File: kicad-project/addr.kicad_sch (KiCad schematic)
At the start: 0 parts

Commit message: address register and more
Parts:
- added U? (x2): 74LS173, symbol 74xx:74LS173
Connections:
- new net: U?.10 (E2), U?.9 (E1) (x2)
- new net CLK: U?.7 (Cp), U?.7 (Cp)
- new net GND: U?.1 (Oe1), U?.1 (Oe1), U?.2 (Oe2), U?.2 (Oe2), U?.8 (GND), U?.8 (GND)
- new net VCC: U?.16 (VCC), U?.16 (VCC)

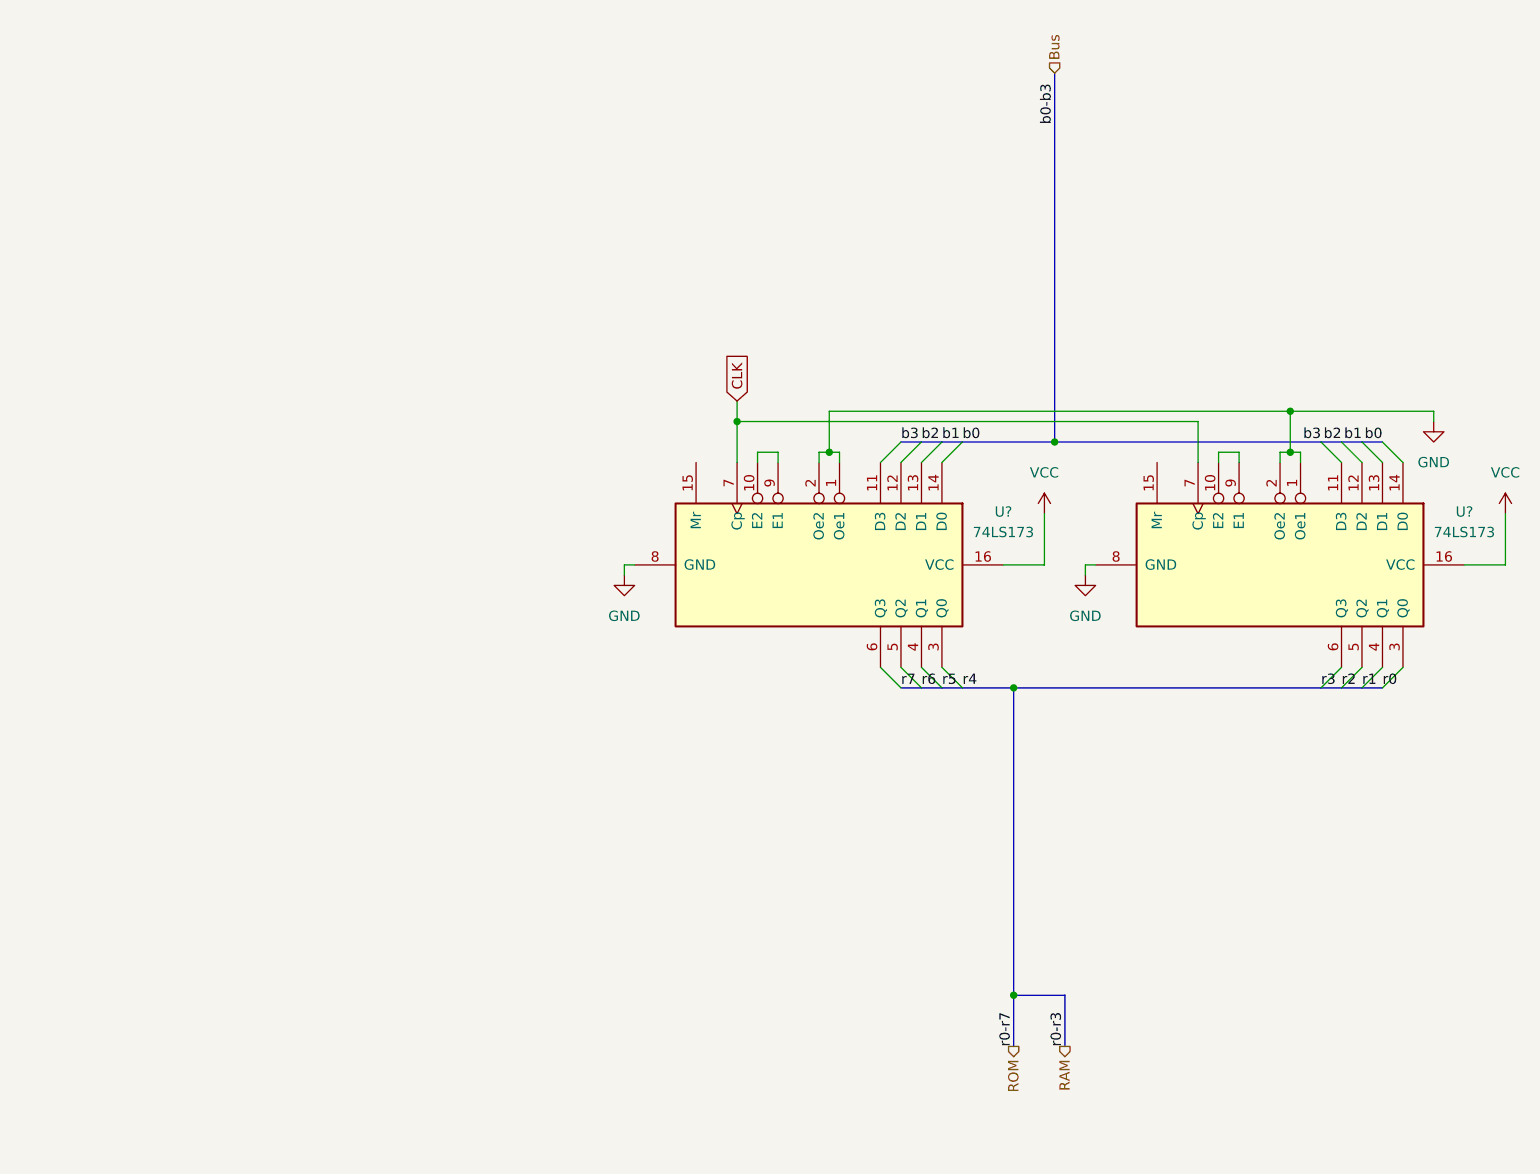
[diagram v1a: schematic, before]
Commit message: update schematic
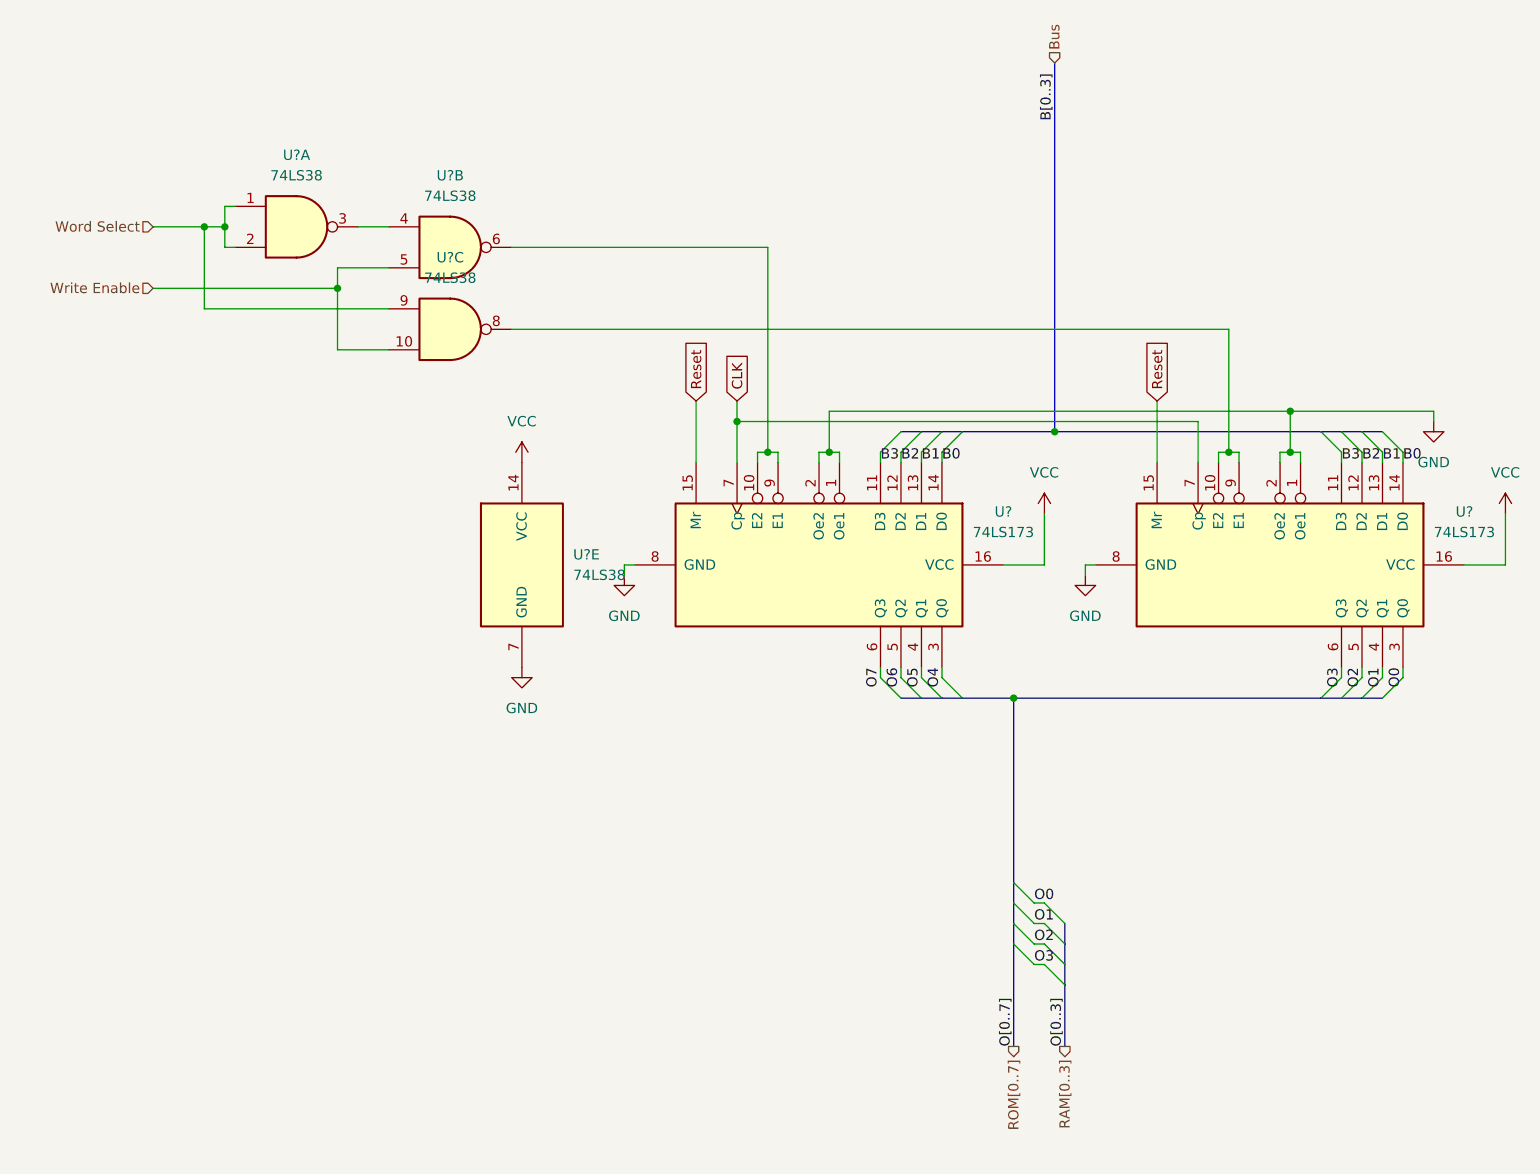
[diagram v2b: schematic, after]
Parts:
- added U? (x4): 74LS38, symbol 74xx:74LS38
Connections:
- net GND: now also U?.7 (GND)
- net VCC: now also U?.14 (VCC)
- net at U?.10 (E2), U?.9 (E1): now also U?.6
- net B3: now reaches U?.11 (D3)
- net B3: now also U?.11 (D3)
- net B2: now reaches U?.12 (D2)
- net B2: now also U?.12 (D2)
- net B1: now reaches U?.13 (D1)
- net B1: now also U?.13 (D1)
- net B0: now reaches U?.14 (D0)
- net B0: now also U?.14 (D0)
- net Reset: now reaches U?.15 (Mr)
- net Reset: now also U?.15 (Mr)
- net O4: now reaches U?.3 (Q0)
- net O5: now reaches U?.4 (Q1)
- net O6: now reaches U?.5 (Q2)
- net O7: now reaches U?.6 (Q3)
- net at U?.10 (E2), U?.9 (E1): now also U?.8
- net O0: now reaches U?.3 (Q0)
- net O1: now reaches U?.4 (Q1)
- net O2: now reaches U?.5 (Q2)
- net O3: now reaches U?.6 (Q3)
- new net: U?.3, U?.4
- new net Word Select: U?.1, U?.2, U?.9
- new net Write Enable: U?.10, U?.5
